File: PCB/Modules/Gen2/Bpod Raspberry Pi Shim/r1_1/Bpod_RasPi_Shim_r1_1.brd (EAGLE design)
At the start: 83.7 x 15.9 mm, 6 parts, among them IC1 SN65HVD31DR, J1 RASPBERRYPI-40-PIN-GPIO_PTH_N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

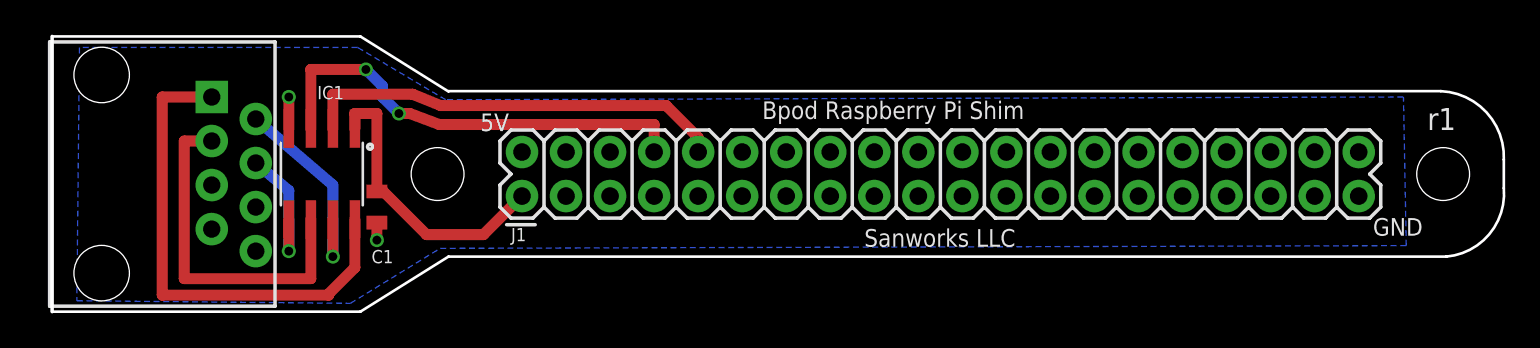
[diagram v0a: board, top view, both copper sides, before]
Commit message: -Updated HiFi module PCB to v1.3. New version pulls unused channel to GND on ADUM5200 isolator, and contains silkscreen instructions for header mounting -Updated Raspberry Pi Shim to v1.1. New version provides more space between RJ45 jack and RS-485 IC for even mounting.
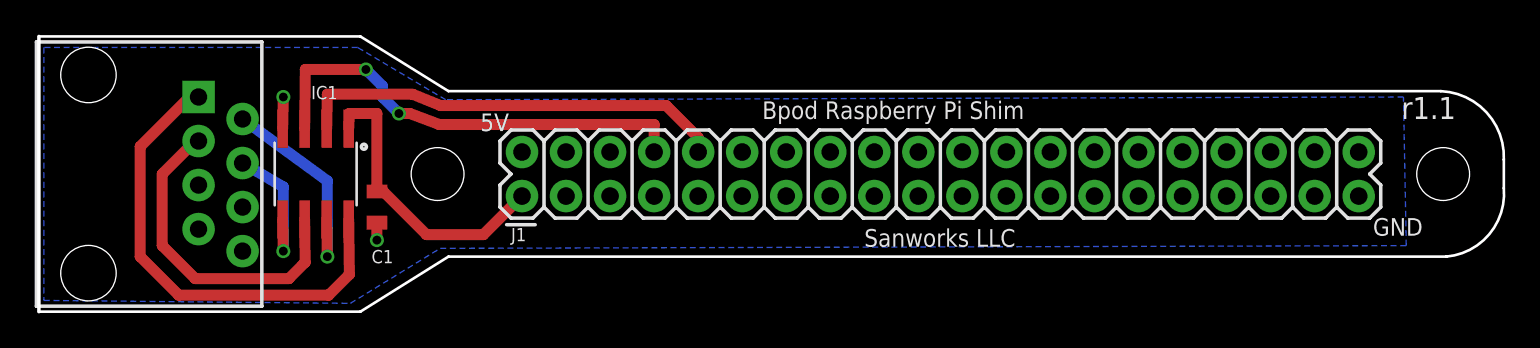
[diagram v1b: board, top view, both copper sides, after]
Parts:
- moved U$2 0.76 mm to (-16.6, 3.81)
- moved IC1 0.36 mm to (-3.53, 3.81)
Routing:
- net N$7: track 28.9 -> 27.6 mm
- net N$9: track 20.2 -> 18.9 mm
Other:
- board size 83.7 x 15.9 mm -> 84.5 x 15.9 mm
- board text added: "r1.1"
- board text removed: "r1"
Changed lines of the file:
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@@
 <?xml version="1.0" encoding="utf-8"?>
 <!DOCTYPE eagle SYSTEM "eagle.dtd">
-<eagle version="9.3.1">
+<eagle version="9.6.2">
 <drawing>
 <settings>
@@
 <wire x1="61.365" y1="8.5925" x2="4.1275" y2="8.5925" width="0.1524" layer="20"/>
 <text x="22.225" y="6.985" size="1.016" layer="21" font="vector" ratio="10">Bpod Raspberry Pi Shim</text>
-<text x="62.23" y="7.62" size="1.27" layer="21" font="vector" ratio="10" rot="R180">r1</text>
+<text x="62.23" y="8.255" size="1.27" layer="21" font="vector" ratio="10" rot="R180">r1.1</text>
 <text x="36.83" y="0.635" size="1.016" layer="21" font="vector" ratio="10" rot="R180">Sanworks LLC</text>
 <text x="7.62" y="7.3025" size="1.016" layer="21" font="vector" ratio="10" rot="R180">5V</text>
 <text x="60.325" y="1.27" size="1.016" layer="21" font="vector" ratio="10" rot="R180">GND</text>
-<wire x1="-0.9525" y1="11.7475" x2="-18.7325" y2="11.7475" width="0.1524" layer="20"/>
-<wire x1="-18.7325" y1="11.7475" x2="-18.7325" y2="-4.1275" width="0.2032" layer="20"/>
-<wire x1="-18.7325" y1="-4.1275" x2="-0.9525" y2="-4.1275" width="0.1524" layer="20"/>
+<wire x1="-0.9525" y1="11.7475" x2="-19.4945" y2="11.7475" width="0.1524" layer="20"/>
+<wire x1="-19.4945" y1="11.7475" x2="-19.4945" y2="-4.1275" width="0.2032" layer="20"/>
+<wire x1="-19.4945" y1="-4.1275" x2="-0.9525" y2="-4.1275" width="0.1524" layer="20"/>
 <wire x1="-0.9525" y1="-4.1275" x2="4.1275" y2="-0.9525" width="0.1524" layer="20"/>
-<wire x1="-0.9525" y1="11.7475" x2="4.1275" y2="8.5725" width="0.1524" layer="20"/>
+<wire x1="-0.9525" y1="11.7475" x2="4.1275" y2="8.5925" width="0.1524" layer="20"/>
 </plain>
 <attributes>
@@
 </class>
 </classes>
-<designrules name="SeeedStudio_2layer_DRU_no_angle_20140221 *">
+<designrules name="SeeedStudio_2layer_DRU_no_angle_20140221">
 <description language="de">&lt;b&gt;EAGLE Design Rules&lt;/b&gt;
 &lt;p&gt;
@@
 <param name="mtCopper" value="0.035mm 0.0175mm 0.035mm 0.035mm 0.035mm 0.035mm 0.035mm 0.035mm 0.035mm 0.035mm 0.035mm 0.035mm 0.035mm 0.035mm 0.0175mm 0.035mm"/>
 <param name="mtIsolate" value="1.5mm 1.1mm 0.2mm 0.15mm 0.2mm 0.15mm 0.2mm 0.15mm 0.2mm 0.15mm 0.2mm 0.15mm 0.2mm 0.15mm 0.2mm"/>
-<param name="mdWireWire" value="12mil"/>
-<param name="mdWirePad" value="12mil"/>
-<param name="mdWireVia" value="12mil"/>
-<param name="mdPadPad" value="12mil"/>
-<param name="mdPadVia" value="12mil"/>
-<param name="mdViaVia" value="12mil"/>
+<param name="mdWireWire" value="6mil"/>
+<param name="mdWirePad" value="6mil"/>
+<param name="mdWireVia" value="6mil"/>
+<param name="mdPadPad" value="6mil"/>
+<param name="mdPadVia" value="6mil"/>
+<param name="mdViaVia" value="6mil"/>
 <param name="mdSmdPad" value="0mil"/>
 <param name="mdSmdVia" value="0mil"/>
@@
 <element name="H3" library="SparkFun-Hardware" package="STAND-OFF-TIGHT" value="STAND-OFFTIGHT" x="3.5" y="3.81" smashed="yes" rot="R90"/>
 <element name="H4" library="SparkFun-Hardware" package="STAND-OFF-TIGHT" value="STAND-OFFTIGHT" x="61.5" y="3.81" smashed="yes" rot="R90"/>
-<element name="U$2" library="SparkFun" package="RJ45-8" value="RJ45-8PTH" x="-15.875" y="3.81" smashed="yes" rot="R270"/>
-<element name="IC1" library="Joshparts4" package="SO08" value="SN65HVD31DR" x="-3.175" y="3.81" smashed="yes" rot="R180">
-<attribute name="NAME" x="-1.905" y="8.89" size="0.762" layer="25" font="vector" ratio="12" rot="R180"/>
+<element name="U$2" library="SparkFun" package="RJ45-8" value="RJ45-8PTH" x="-16.637" y="3.81" smashed="yes" rot="R270"/>
+<element name="IC1" library="Joshparts4" package="SO08" value="SN65HVD31DR" x="-3.5306" y="3.81" smashed="yes" rot="R180">
+<attribute name="NAME" x="-2.2606" y="8.89" size="0.762" layer="25" font="vector" ratio="12" rot="R180"/>
 </element>
 <element name="C1" library="SparkFun-Capacitors" package="0805" value="0.1uF" x="0" y="1.905" smashed="yes" rot="R90">
@@
 <vertex x="3.96875" y="8.09625"/>
 <vertex x="-1.11125" y="11.1125"/>
-<vertex x="-17.154071875" y="11.1125"/>
-<vertex x="-17.307075" y="-3.497003125"/>
+<vertex x="-19.211884375" y="11.1125"/>
+<vertex x="-19.211884375" y="-3.4788625"/>
 <vertex x="-1.529275" y="-3.64726875"/>
 <vertex x="3.65125" y="-0.47625"/>
@@
 <wire x1="0" y1="1.005" x2="0" y2="0" width="0.635" layer="1"/>
 <via x="0" y="0" extent="1-16" drill="0.508"/>
-<wire x1="-5.08" y1="6.4262" x2="-5.08" y2="8.255" width="0.635" layer="1"/>
-<via x="-5.08" y="8.255" extent="1-16" drill="0.508"/>
+<wire x1="-5.3975" y1="8.255" x2="-5.4356" y2="6.4262" width="0.635" layer="1"/>
+<via x="-5.3975" y="8.255" extent="1-16" drill="0.508"/>
 </signal>
 <signal name="SDA">
@@
 <wire x1="0.3175" y1="8.89" x2="-0.635" y2="9.8425" width="0.635" layer="16"/>
 <via x="-0.635" y="9.8425" extent="1-16" drill="0.508"/>
-<wire x1="-0.635" y1="9.8425" x2="-3.81" y2="9.8425" width="0.635" layer="1"/>
-<wire x1="-3.81" y1="9.8425" x2="-3.81" y2="6.4262" width="0.635" layer="1"/>
+<wire x1="-0.635" y1="9.8425" x2="-4.1275" y2="9.8425" width="0.635" layer="1"/>
+<wire x1="-4.1275" y1="9.8425" x2="-4.1656" y2="6.4262" width="0.635" layer="1"/>
 </signal>
 <signal name="RX1">
@@
 <wire x1="16.68685" y1="7.76065" x2="3.671265625" y2="7.76065" width="0.635" layer="1"/>
 <wire x1="3.671265625" y1="7.76065" x2="2.06375" y2="8.41375" width="0.635" layer="1"/>
-<wire x1="2.06375" y1="8.41375" x2="-2.54" y2="8.41375" width="0.635" layer="1"/>
-<wire x1="-2.54" y1="8.41375" x2="-2.54" y2="6.4262" width="0.635" layer="1"/>
+<wire x1="2.06375" y1="8.41375" x2="-2.8575" y2="8.41375" width="0.635" layer="1"/>
+<wire x1="-2.8575" y1="8.41375" x2="-2.8956" y2="6.4262" width="0.635" layer="1"/>
 </signal>
 <signal name="N$7">
 <contactref element="IC1" pad="8"/>
 <contactref element="U$2" pad="1"/>
-<wire x1="-1.27" y1="1.1938" x2="-1.27" y2="-1.5875" width="0.635" layer="1"/>
-<wire x1="-1.27" y1="-1.5875" x2="-2.8194" y2="-3.1369" width="0.635" layer="1"/>
-<wire x1="-2.8194" y1="-3.1369" x2="-2.7813" y2="-3.175" width="0.635" layer="1"/>
-<wire x1="-2.7813" y1="-3.175" x2="-12.3825" y2="-3.175" width="0.635" layer="1"/>
-<wire x1="-12.3825" y1="-3.175" x2="-12.3825" y2="8.255" width="0.635" layer="1"/>
-<wire x1="-12.3825" y1="8.255" x2="-9.525" y2="8.255" width="0.635" layer="1"/>
+<wire x1="-1.6256" y1="1.1938" x2="-1.586575" y2="-1.980275" width="0.635" layer="1"/>
+<wire x1="-1.586575" y1="-1.980275" x2="-2.7813" y2="-3.175" width="0.635" layer="1"/>
+<wire x1="-2.7813" y1="-3.175" x2="-11.43" y2="-3.175" width="0.635" layer="1"/>
+<wire x1="-11.43" y1="-3.175" x2="-13.6525" y2="-0.9525" width="0.635" layer="1"/>
+<wire x1="-13.6525" y1="-0.9525" x2="-13.6525" y2="5.3975" width="0.635" layer="1"/>
+<wire x1="-13.6525" y1="5.3975" x2="-10.795" y2="8.255" width="0.635" layer="1"/>
+<wire x1="-10.795" y1="8.255" x2="-10.287" y2="8.255" width="0.635" layer="1"/>
 </signal>
 <signal name="N$8">
 <contactref element="U$2" pad="2"/>
 <contactref element="IC1" pad="7"/>
-<wire x1="-2.54" y1="1.1938" x2="-2.54" y2="-0.9525" width="0.635" layer="1"/>
-<via x="-2.54" y="-0.9525" extent="1-16" drill="0.508"/>
-<wire x1="-2.54" y1="-0.9525" x2="-2.54" y2="3.175" width="0.635" layer="16"/>
-<wire x1="-2.54" y1="3.175" x2="-6.985" y2="6.985" width="0.635" layer="16"/>
+<wire x1="-2.8956" y1="1.1938" x2="-2.8575" y2="-0.9525" width="0.635" layer="1"/>
+<via x="-2.8575" y="-0.9525" extent="1-16" drill="0.508"/>
+<wire x1="-2.8575" y1="-0.9525" x2="-2.8575" y2="3.41923125" width="0.635" layer="16"/>
+<wire x1="-2.8575" y1="3.41923125" x2="-7.747" y2="6.985" width="0.635" layer="16"/>
 </signal>
 <signal name="N$9">
 <contactref element="U$2" pad="3"/>
 <contactref element="IC1" pad="6"/>
-<wire x1="-3.81" y1="1.1938" x2="-3.81" y2="-2.2225" width="0.635" layer="1"/>
-<wire x1="-3.81" y1="-2.2225" x2="-11.1125" y2="-2.2225" width="0.635" layer="1"/>
-<wire x1="-11.1125" y1="-2.2225" x2="-11.1125" y2="5.715" width="0.635" layer="1"/>
-<wire x1="-11.1125" y1="5.715" x2="-9.525" y2="5.715" width="0.635" layer="1"/>
+<wire x1="-4.1656" y1="1.1938" x2="-4.13804375" y2="-1.277078125" width="0.635" layer="1"/>
+<wire x1="-4.13804375" y1="-1.277078125" x2="-5.072959375" y2="-2.2225" width="0.635" layer="1"/>
+<wire x1="-5.072959375" y1="-2.2225" x2="-10.4775" y2="-2.2225" width="0.635" layer="1"/>
+<wire x1="-10.4775" y1="-2.2225" x2="-12.3825" y2="-0.3175" width="0.635" layer="1"/>
+<wire x1="-12.3825" y1="-0.3175" x2="-12.3825" y2="3.81" width="0.635" layer="1"/>
+<wire x1="-12.3825" y1="3.81" x2="-10.4775" y2="5.715" width="0.635" layer="1"/>
+<wire x1="-10.4775" y1="5.715" x2="-10.287" y2="5.715" width="0.635" layer="1"/>
 </signal>
 <signal name="N$10">
 <contactref element="U$2" pad="4"/>
 <contactref element="IC1" pad="5"/>
-<wire x1="-5.08" y1="1.1938" x2="-5.08" y2="-0.635" width="0.635" layer="1"/>
-<via x="-5.08" y="-0.635" extent="1-16" drill="0.508"/>
-<wire x1="-5.08" y1="-0.635" x2="-5.08" y2="2.8575" width="0.635" layer="16"/>
-<wire x1="-5.08" y1="2.8575" x2="-6.985" y2="4.445" width="0.635" layer="16"/>
+<wire x1="-5.4356" y1="1.1938" x2="-5.3975" y2="-0.635" width="0.635" layer="1"/>
+<via x="-5.3975" y="-0.635" extent="1-16" drill="0.508"/>
+<wire x1="-5.3975" y1="-0.635" x2="-5.3975" y2="3.06638125" width="0.635" layer="16"/>
+<wire x1="-5.3975" y1="3.06638125" x2="-7.747" y2="4.445" width="0.635" layer="16"/>
 </signal>
 <signal name="VCC">
@@
 <wire x1="0" y1="2.805" x2="0.37" y2="2.805" width="0.635" layer="1"/>
 <wire x1="0" y1="2.805" x2="0" y2="7.3025" width="0.635" layer="1"/>
-<wire x1="0" y1="7.3025" x2="-1.27" y2="7.3025" width="0.635" layer="1"/>
-<wire x1="-1.27" y1="7.3025" x2="-1.27" y2="6.4262" width="0.635" layer="1"/>
+<wire x1="0" y1="7.3025" x2="-1.5875" y2="7.3025" width="0.635" layer="1"/>
+<wire x1="-1.5875" y1="7.3025" x2="-1.6256" y2="6.4262" width="0.635" layer="1"/>
 </signal>
 </signals>
